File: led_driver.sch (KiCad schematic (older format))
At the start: 7 parts, among them U1 SY7200A

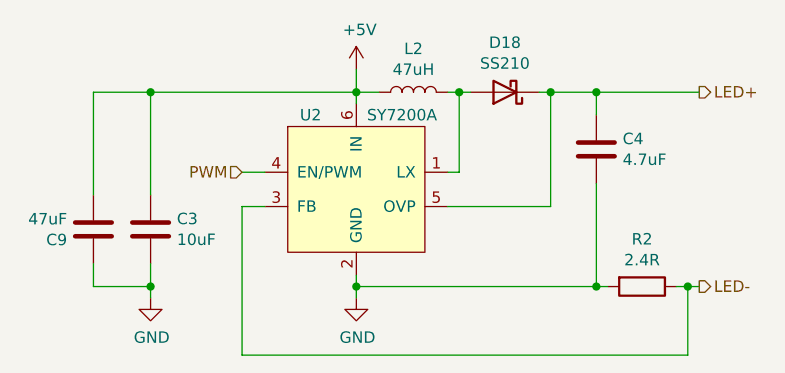
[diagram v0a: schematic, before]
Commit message: Add schematic export
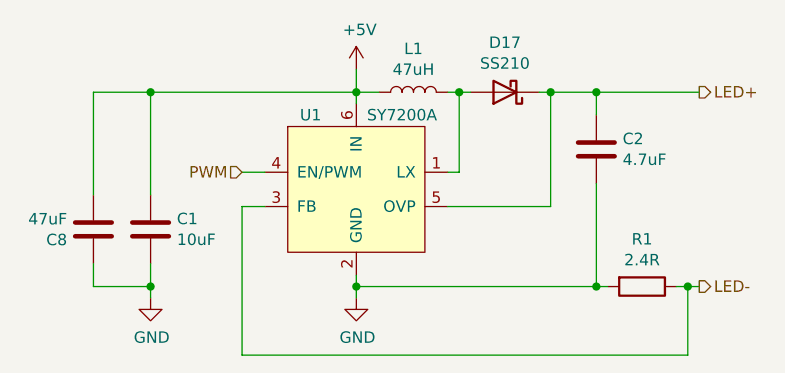
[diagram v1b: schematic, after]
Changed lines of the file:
@@
 $Descr A4 11693 8268
 encoding utf-8
-Sheet 3 3
+Sheet 2 3
 Title ""
 Date ""
@@
 AR Path="/5FED3853/5FED48D9" Ref="U1"  Part="1"
 AR Path="/5FED5055/5FED48D9" Ref="U2"  Part="1"
-F 0 "U2" H 5700 3750 50  0000 C CNN
+F 0 "U1" H 5700 3750 50  0000 C CNN
 F 1 "SY7200A" H 6100 3750 50  0000 C CNN
 F 2 "Package_TO_SOT_SMD:SOT-23-6" H 5900 3450 50  0001 C CNN
@@
 AR Path="/5FED3853/5FED48E0" Ref="D17"  Part="1"
 AR Path="/5FED5055/5FED48E0" Ref="D18"  Part="1"
-F 0 "D18" H 6550 2833 50  0000 C CNN
+F 0 "D17" H 6550 2833 50  0000 C CNN
 F 1 "SS210" H 6550 2924 50  0000 C CNN
 F 2 "Diode_SMD:D_SMA" H 6550 3050 50  0001 C CNN
@@
 AR Path="/5FED3853/5FED48E7" Ref="L1"  Part="1"
 AR Path="/5FED5055/5FED48E7" Ref="L2"  Part="1"
-F 0 "L2" V 6340 3050 50  0000 C CNN
+F 0 "L1" V 6340 3050 50  0000 C CNN
 F 1 "47uH" V 6249 3050 50  0000 C CNN
 F 2 "Inductor_Sunlord:MWSA0603S" H 6150 3050 50  0001 C CNN
@@
 AR Path="/5FED3853/5FED48F8" Ref="R1"  Part="1"
 AR Path="/5FED5055/5FED48F8" Ref="R2"  Part="1"
-F 0 "R2" V 6943 3900 50  0000 C CNN
+F 0 "R1" V 6943 3900 50  0000 C CNN
 F 1 "2.4R" V 7034 3900 50  0000 C CNN
 F 2 "Resistor_SMD:R_0805_2012Metric" V 7080 3900 50  0001 C CNN
@@
 AR Path="/5FED3853/5FED48FF" Ref="C2"  Part="1"
 AR Path="/5FED5055/5FED48FF" Ref="C4"  Part="1"
-F 0 "C4" H 7065 3346 50  0000 L CNN
+F 0 "C2" H 7065 3346 50  0000 L CNN
 F 1 "4.7uF" H 7065 3255 50  0000 L CNN
 F 2 "Capacitor_SMD:C_1206_3216Metric" H 6988 3150 50  0001 C CNN
@@
 AR Path="/5FED3853/5FED4908" Ref="#PWR0101"  Part="1"
 AR Path="/5FED5055/5FED4908" Ref="#PWR0104"  Part="1"
-F 0 "#PWR0104" H 5900 3700 50  0001 C CNN
+F 0 "#PWR0101" H 5900 3700 50  0001 C CNN
 F 1 "GND" H 5905 3777 50  0000 C CNN
 F 2 "" H 5900 3950 50  0001 C CNN
@@
 AR Path="/5FED3853/5FED491B" Ref="C1"  Part="1"
 AR Path="/5FED5055/5FED491B" Ref="C3"  Part="1"
-F 0 "C3" H 5115 3696 50  0000 L CNN
+F 0 "C1" H 5115 3696 50  0000 L CNN
 F 1 "10uF" H 5115 3605 50  0000 L CNN
 F 2 "Capacitor_SMD:C_0805_2012Metric" H 5038 3500 50  0001 C CNN
@@
 AR Path="/5FED3853/5FED4921" Ref="#PWR0102"  Part="1"
 AR Path="/5FED5055/5FED4921" Ref="#PWR0105"  Part="1"
-F 0 "#PWR0105" H 5000 3700 50  0001 C CNN
+F 0 "#PWR0102" H 5000 3700 50  0001 C CNN
 F 1 "GND" H 5005 3777 50  0000 C CNN
 F 2 "" H 5000 3950 50  0001 C CNN
@@
 AR Path="/5FED3853/5FED492D" Ref="#PWR0103"  Part="1"
 AR Path="/5FED5055/5FED492D" Ref="#PWR0106"  Part="1"
-F 0 "#PWR0106" H 5900 2800 50  0001 C CNN
+F 0 "#PWR0103" H 5900 2800 50  0001 C CNN
 F 1 "+5V" H 5915 3123 50  0000 C CNN
 F 2 "" H 5900 2950 50  0001 C CNN
@@
 AR Path="/5FED3853/5FF331F8" Ref="C8"  Part="1"
 AR Path="/5FED5055/5FF331F8" Ref="C9"  Part="1"
-F 0 "C9" H 4865 3696 50  0000 L CNN
+F 0 "C8" H 4865 3696 50  0000 L CNN
 F 1 "47uF" H 4865 3605 50  0000 L CNN
 F 2 "Capacitor_SMD:C_1206_3216Metric" H 4788 3500 50  0001 C CNN
